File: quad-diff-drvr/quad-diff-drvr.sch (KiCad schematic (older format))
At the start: 43 parts, among them J1 Raspberry_Pi_2_3, J2 Conn_01x04, J3 Conn_01x04, J4 Conn_01x04, J5 Conn_01x04, J6 Conn_01x04, U1 INA3221, U2 74LS153, U3 74LS153, U4 74LS153, U5 PCA9555PW

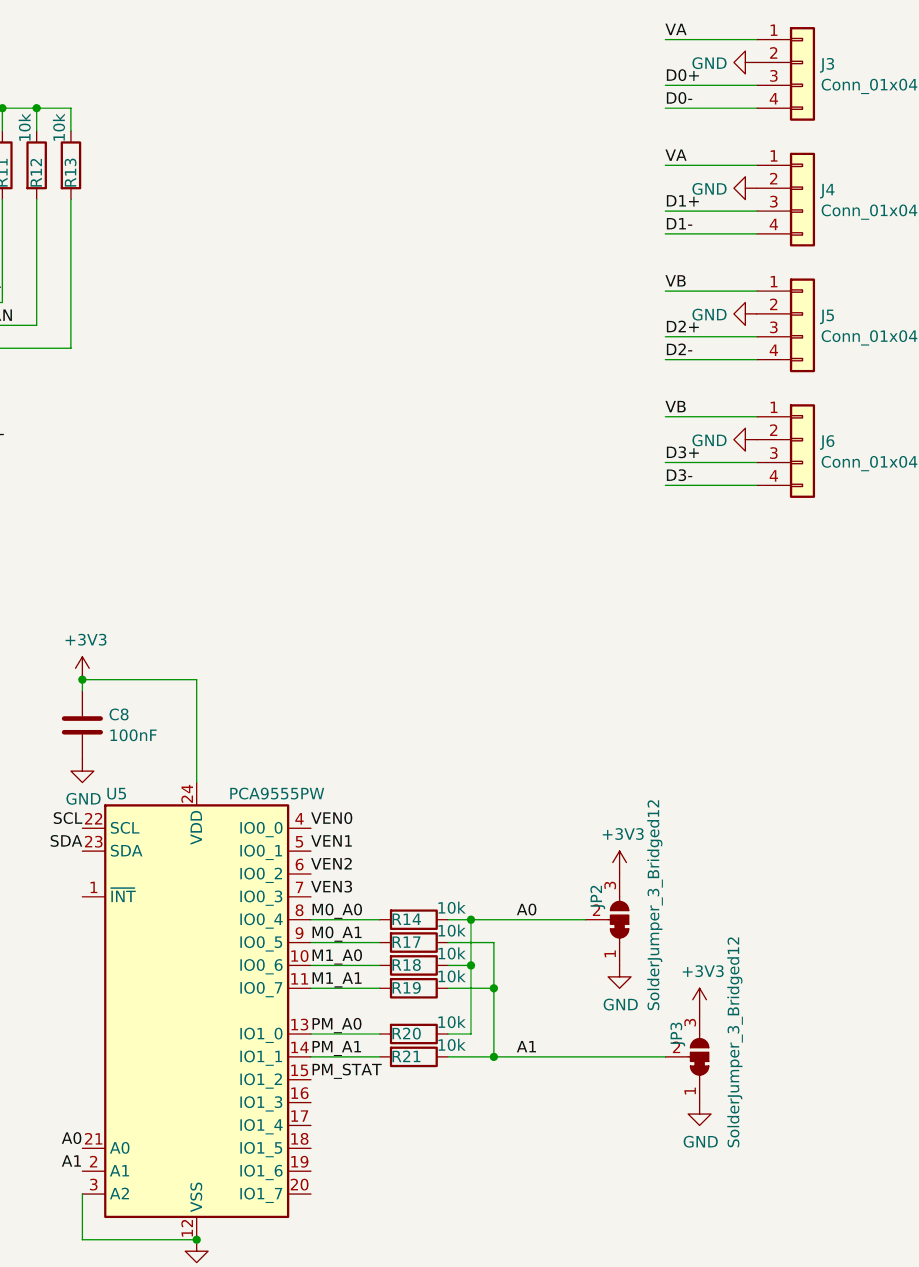
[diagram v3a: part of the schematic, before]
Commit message: qdd: driver added
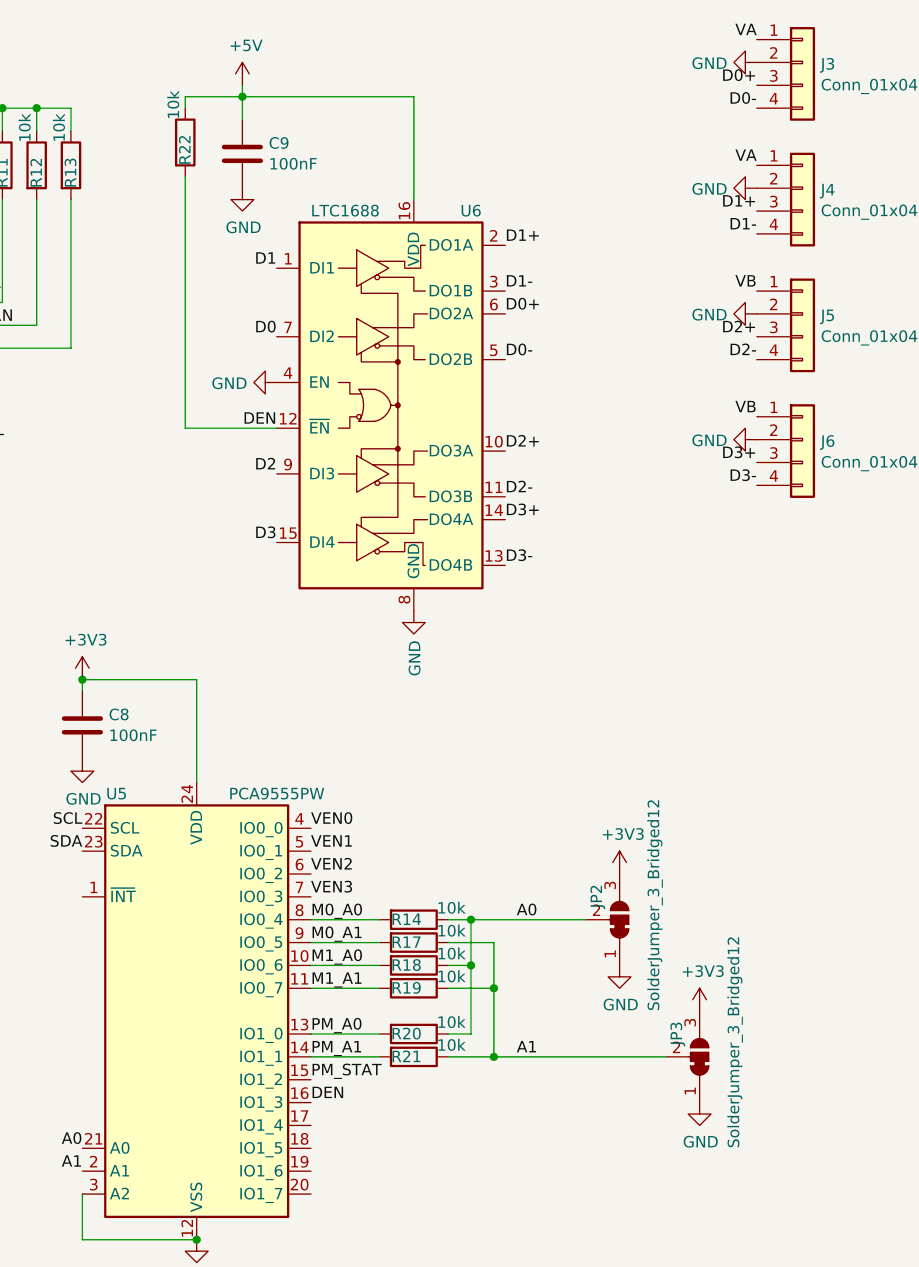
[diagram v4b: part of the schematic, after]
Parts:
- added C9: 100nF, Capacitor_SMD:C_0603_1608Metric, symbol Device:C
- added R22: 10k, Resistor_SMD:R_0603_1608Metric, symbol Device:R
- added U6: LTC1688, Package_SO:SOIC-16_3.9x9.9mm_P1.27mm, symbol Interface:LTC1688
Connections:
- net +5V: now also C9.1, R22.1, U6.16 (VDD)
- net D0: now also U6.7 (DI2)
- net D0+: now also U6.6 (DO2A)
- net D0-: now also U6.5 (DO2B)
- net D1: now also U6.1 (DI1)
- net D1+: now also U6.2 (DO1A)
- net D1-: now also U6.3 (DO1B)
- net D2: now also U6.9 (DI3)
- net D2+: now also U6.10 (DO3A)
- net D2-: now also U6.11 (DO3B)
- net D3: now also U6.15 (DI4)
- net D3+: now also U6.14 (DO4A)
- net D3-: now also U6.13 (DO4B)
- net GND: now also C9.2, U6.4 (EN), U6.8 (GND)
- net DEN: now reaches U5.16 (IO1_3)
- net DEN: now also R22.2, U6.12 (~EN)
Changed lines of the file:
@@
 Wire Wire Line
 	3700 850  3700 950
-Wire Wire Line
-	10750 650  10350 650
-Text Label 10350 650  0    50   ~ 0
+Text Label 10750 650  2    50   ~ 0
 VA
-Wire Wire Line
-	10750 850  10350 850
-Text Label 10350 850  0    50   ~ 0
+Text Label 10750 850  2    50   ~ 0
 D0+
-Wire Wire Line
-	10750 950  10350 950
-Text Label 10350 950  0    50   ~ 0
+Text Label 10750 950  2    50   ~ 0
 D0-
 $Comp
@@
 	0    1    1    0
 $EndComp
-Wire Wire Line
-	10750 1200 10350 1200
-Text Label 10350 1200 0    50   ~ 0
+Text Label 10750 1200 2    50   ~ 0
 VA
-Wire Wire Line
-	10750 1400 10350 1400
-Text Label 10350 1400 0    50   ~ 0
+Text Label 10750 1400 2    50   ~ 0
 D1+
-Wire Wire Line
-	10750 1500 10350 1500
-Text Label 10350 1500 0    50   ~ 0
+Text Label 10750 1500 2    50   ~ 0
 D1-
 $Comp
@@
 	0    1    1    0
 $EndComp
-Wire Wire Line
-	10750 1750 10350 1750
-Text Label 10350 1750 0    50   ~ 0
+Text Label 10750 1750 2    50   ~ 0
 VB
-Wire Wire Line
-	10750 1950 10350 1950
-Text Label 10350 1950 0    50   ~ 0
+Text Label 10750 1950 2    50   ~ 0
 D2+
-Wire Wire Line
-	10750 2050 10350 2050
-Text Label 10350 2050 0    50   ~ 0
+Text Label 10750 2050 2    50   ~ 0
 D2-
 $Comp
@@
 	0    1    1    0
 $EndComp
-Wire Wire Line
-	10750 2300 10350 2300
-Text Label 10350 2300 0    50   ~ 0
+Text Label 10750 2300 2    50   ~ 0
 VB
-Wire Wire Line
-	10750 2500 10350 2500
-Text Label 10350 2500 0    50   ~ 0
+Text Label 10750 2500 2    50   ~ 0
 D3+
-Wire Wire Line
-	10750 2600 10350 2600
-Text Label 10350 2600 0    50   ~ 0
+Text Label 10750 2600 2    50   ~ 0
 D3-
 $Comp
@@
 Text Label 9700 5100 0    50   ~ 0
 A1
+$Comp
+L Interface:LTC1688 U6
+U 1 1 61ED37CD
+P 9150 2250
+F 0 "U6" H 9500 3100 50  0000 C CNN
+F 1 "LTC1688" H 8950 3100 50  0000 C CNN
+F 2 "Package_SO:SOIC-16_3.9x9.9mm_P1.27mm" H 10150 1400 50  0001 C CNN
+F 3 "https://www.analog.com/media/en/technical-documentation/data-sheets/16889fa.pdf" H 9150 2150 50  0001 C CNN
+	1    9150 2250
+	1    0    0    -1
+$EndComp
+Text Label 8800 5300 0    50   ~ 0
+DEN
+Text Label 8650 2350 2    50   ~ 0
+DEN
+Text Label 9650 1550 0    50   ~ 0
+D1+
+Text Label 9650 1750 0    50   ~ 0
+D1-
+Text Label 9650 1850 0    50   ~ 0
+D0+
+Text Label 9650 2050 0    50   ~ 0
+D0-
+Text Label 9650 2450 0    50   ~ 0
+D2+
+Text Label 9650 2650 0    50   ~ 0
+D2-
+Text Label 9650 2750 0    50   ~ 0
+D3+
+Text Label 9650 2950 0    50   ~ 0
+D3-
+$Comp
+L power:GND #PWR0136
+U 1 1 61F139AF
+P 9250 3150
+F 0 "#PWR0136" H 9250 2900 50  0001 C CNN
+F 1 "GND" V 9255 3022 50  0000 R CNN
+F 2 "" H 9250 3150 50  0001 C CNN
+F 3 "" H 9250 3150 50  0001 C CNN
+	1    9250 3150
+	1    0    0    -1
+$EndComp
+$Comp
+L power:GND #PWR0137
+U 1 1 61F13FCA
+P 8650 2150
+F 0 "#PWR0137" H 8650 1900 50  0001 C CNN
+F 1 "GND" V 8655 2022 50  0000 R CNN
+F 2 "" H 8650 2150 50  0001 C CNN
+F 3 "" H 8650 2150 50  0001 C CNN
+	1    8650 2150
+	0    1    1    0
+$EndComp
+$Comp
+L Device:C C9
+U 1 1 61F15C69
+P 8500 1150
+F 0 "C9" H 8615 1196 50  0000 L CNN
+F 1 "100nF" H 8615 1105 50  0000 L CNN
+F 2 "Capacitor_SMD:C_0603_1608Metric" H 8538 1000 50  0001 C CNN
+F 3 "~" H 8500 1150 50  0001 C CNN
+	1    8500 1150
+	1    0    0    -1
+$EndComp
+$Comp
+L power:GND #PWR0138
+U 1 1 61F164E1
+P 8500 1300
+F 0 "#PWR0138" H 8500 1050 50  0001 C CNN
+F 1 "GND" H 8505 1127 50  0000 C CNN
+F 2 "" H 8500 1300 50  0001 C CNN
+F 3 "" H 8500 1300 50  0001 C CNN
+	1    8500 1300
+	1    0    0    -1
+$EndComp
+Wire Wire Line
+	9250 1350 9250 900
+Wire Wire Line
+	9250 900  8500 900
+Wire Wire Line
+	8500 900  8500 1000
+$Comp
+L power:+5V #PWR0139
+U 1 1 61F35BF0
+P 8500 850
+F 0 "#PWR0139" H 8500 700 50  0001 C CNN
+F 1 "+5V" H 8515 1023 50  0000 C CNN
+F 2 "" H 8500 850 50  0001 C CNN
+F 3 "" H 8500 850 50  0001 C CNN
+	1    8500 850
+	1    0    0    -1
+$EndComp
+Wire Wire Line
+	8500 850  8500 900
+Connection ~ 8500 900
+Text Label 8650 1650 2    50   ~ 0
+D1
+Text Label 8650 1950 2    50   ~ 0
+D0
+Text Label 8650 2550 2    50   ~ 0
+D2
+Text Label 8650 2850 2    50   ~ 0
+D3
+$Comp
+L Device:R R22
+U 1 1 61F5B30A
+P 8250 1100
+F 0 "R22" V 8250 1000 50  0000 L CNN
+F 1 "10k" V 8200 1200 50  0000 L CNN
+F 2 "Resistor_SMD:R_0603_1608Metric" V 8180 1100 50  0001 C CNN
+F 3 "~" H 8250 1100 50  0001 C CNN
+	1    8250 1100
+	1    0    0    -1
+$EndComp
+Wire Wire Line
+	8500 900  8250 900
+Wire Wire Line
+	8250 900  8250 950
+Wire Wire Line
+	8650 2350 8250 2350
+Wire Wire Line
+	8250 2350 8250 1250
 $EndSCHEMATC

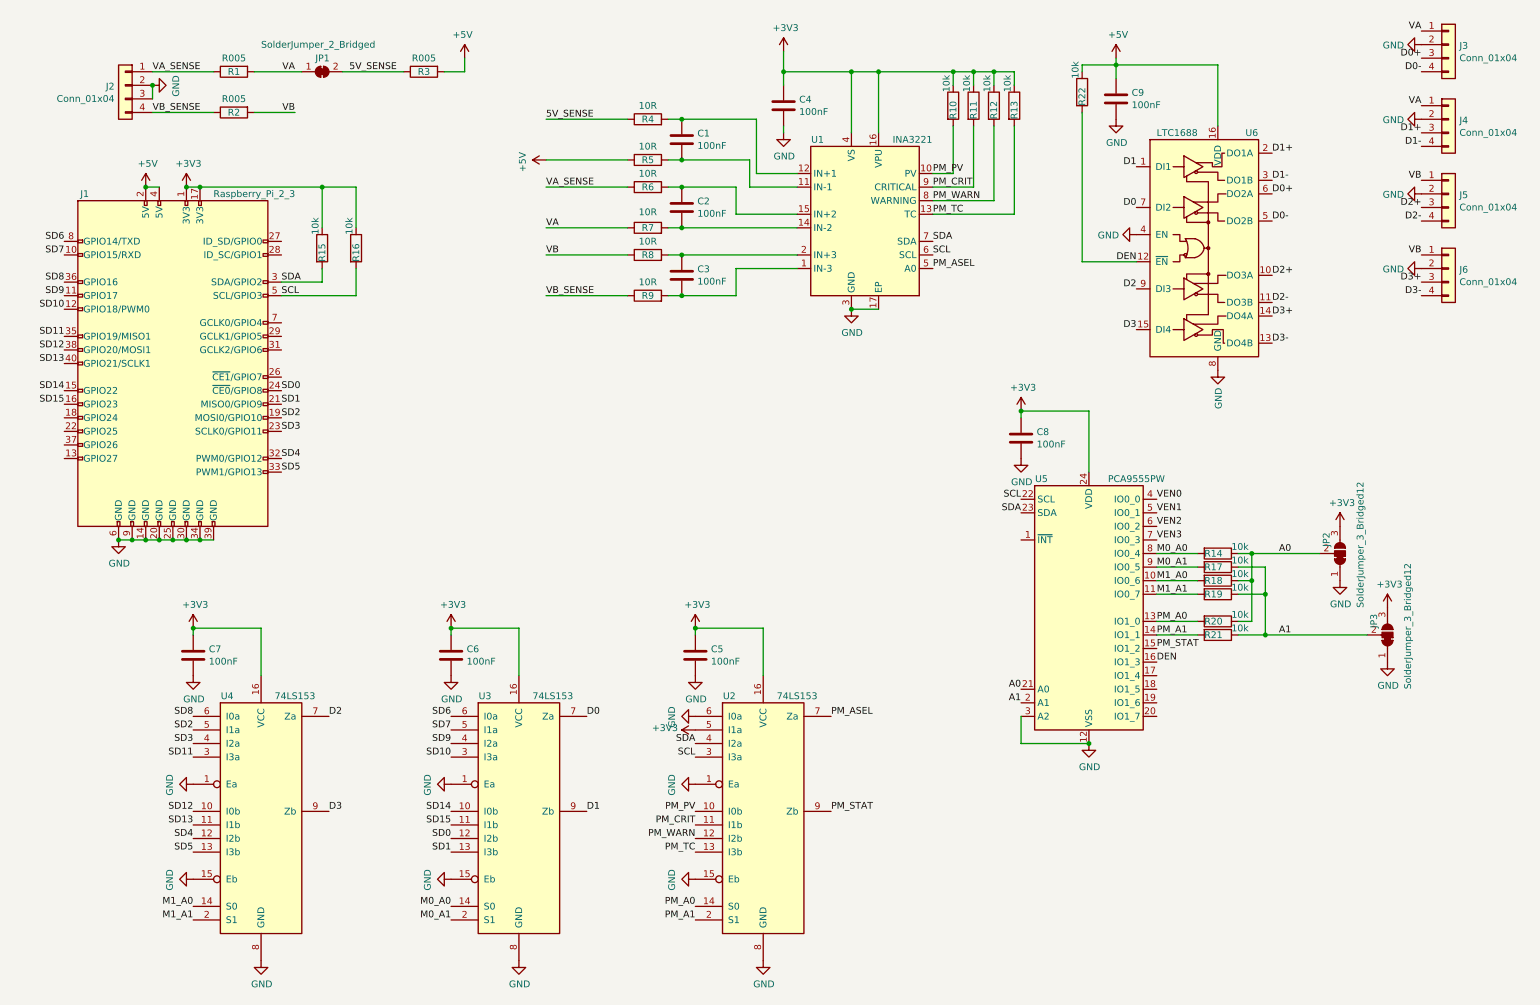
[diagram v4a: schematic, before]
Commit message: qdd: first pass at routing
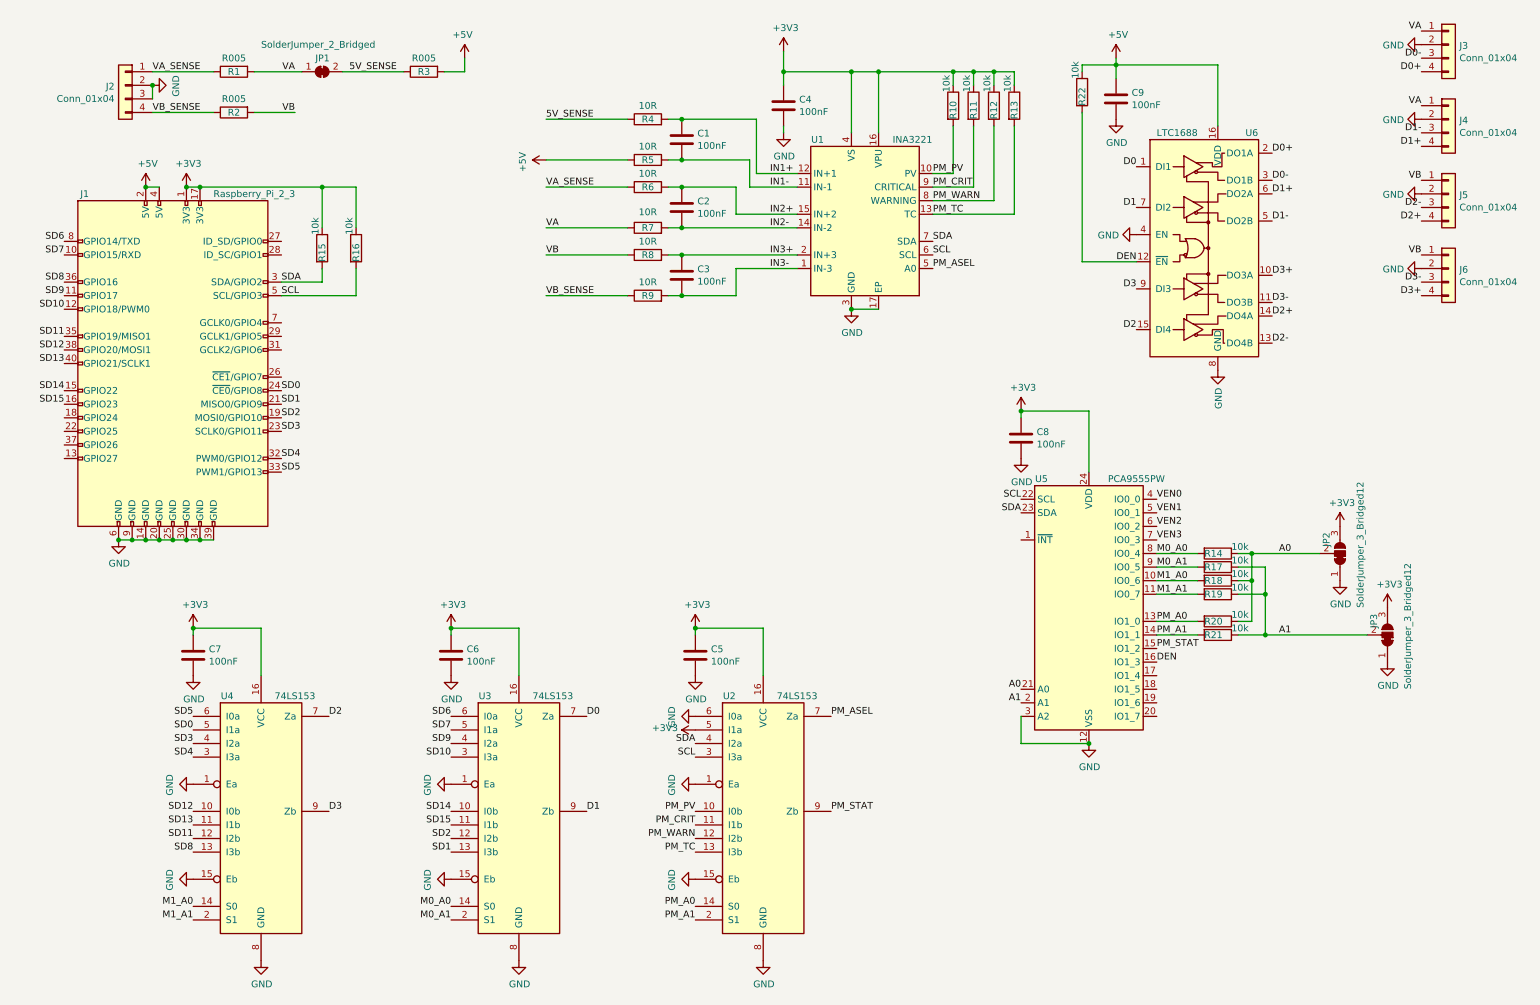
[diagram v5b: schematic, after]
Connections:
- net D0: now also U6.1 (DI1); no longer U6.7 (DI2)
- net D0+: now also J3.4 (Pin_4), U6.2 (DO1A); no longer J3.3 (Pin_3), U6.6 (DO2A)
- net D0-: now also J3.3 (Pin_3), U6.3 (DO1B); no longer J3.4 (Pin_4), U6.5 (DO2B)
- net D1: now also U6.7 (DI2); no longer U6.1 (DI1)
- net D1+: now also J4.4 (Pin_4), U6.6 (DO2A); no longer J4.3 (Pin_3), U6.2 (DO1A)
- net D1-: now also J4.3 (Pin_3), U6.5 (DO2B); no longer J4.4 (Pin_4), U6.3 (DO1B)
- net D2: now also U6.15 (DI4); no longer U6.9 (DI3)
- net D2+: now also J5.4 (Pin_4), U6.14 (DO4A); no longer J5.3 (Pin_3), U6.10 (DO3A)
- net D2-: now also J5.3 (Pin_3), U6.13 (DO4B); no longer J5.4 (Pin_4), U6.11 (DO3B)
- net D3: now also U6.9 (DI3); no longer U6.15 (DI4)
- net D3+: now also J6.4 (Pin_4), U6.10 (DO3A); no longer J6.3 (Pin_3), U6.14 (DO4A)
- net D3-: now also J6.3 (Pin_3), U6.11 (DO3B); no longer J6.4 (Pin_4), U6.13 (DO4B)
- net SD0: now also U4.5 (I1a); no longer U3.12 (I2b)
- net SD11: now also U4.12 (I2b); no longer U4.3 (I3a)
- net SD2: now also U3.12 (I2b); no longer U4.5 (I1a)
- net SD4: now also U4.3 (I3a); no longer U4.12 (I2b)
- net SD5: now also U4.6 (I0a); no longer U4.13 (I3b)
- net SD8: now also U4.13 (I3b); no longer U4.6 (I0a)
- net IN3-: now reaches C3.2, R9.2, U1.1 (IN-3)
- net IN1-: now reaches C1.2, R5.2, U1.11 (IN-1)
- net IN1+: now reaches C1.1, R4.2, U1.12 (IN+1)
- net IN2-: now reaches C2.2, R7.2, U1.14 (IN-2)
- net IN2+: now reaches C2.1, R6.2, U1.15 (IN+2)
- net IN3+: now reaches C3.1, R8.2, U1.2 (IN+3)
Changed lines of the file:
@@
 Text Label 10750 650  2    50   ~ 0
 VA
+Text Label 10750 950  2    50   ~ 0
+D0+
 Text Label 10750 850  2    50   ~ 0
-D0+
-Text Label 10750 950  2    50   ~ 0
 D0-
 $Comp
@@
 Text Label 10750 1200 2    50   ~ 0
 VA
+Text Label 10750 1500 2    50   ~ 0
+D1+
 Text Label 10750 1400 2    50   ~ 0
-D1+
-Text Label 10750 1500 2    50   ~ 0
 D1-
 $Comp
@@
 Text Label 10750 1750 2    50   ~ 0
 VB
+Text Label 10750 2050 2    50   ~ 0
+D2+
 Text Label 10750 1950 2    50   ~ 0
-D2+
-Text Label 10750 2050 2    50   ~ 0
 D2-
 $Comp
@@
 Text Label 10750 2300 2    50   ~ 0
 VB
+Text Label 10750 2600 2    50   ~ 0
+D3+
 Text Label 10750 2500 2    50   ~ 0
-D3+
-Text Label 10750 2600 2    50   ~ 0
 D3-
 $Comp
@@
 Text Label 750  2200 2    50   ~ 0
 SD6
-Text Label 3600 6600 2    50   ~ 0
+Text Label 1700 5800 2    50   ~ 0
 SD0
 Text Label 3600 6700 2    50   ~ 0
 SD1
-Text Label 1700 5800 2    50   ~ 0
+Text Label 3600 6600 2    50   ~ 0
 SD2
 Text Label 1700 5900 2    50   ~ 0
 SD3
-Text Label 1700 6600 2    50   ~ 0
+Text Label 1700 6000 2    50   ~ 0
 SD4
-Text Label 1700 6700 2    50   ~ 0
+Text Label 1700 5700 2    50   ~ 0
 SD5
 Text Label 3600 5800 2    50   ~ 0
@@
 Text Label 2700 6400 0    50   ~ 0
 D3
-Text Label 1700 5700 2    50   ~ 0
+Text Label 1700 6700 2    50   ~ 0
 SD8
 Text Label 3600 5900 2    50   ~ 0
@@
 Text Label 3600 6000 2    50   ~ 0
 SD10
-Text Label 1700 6000 2    50   ~ 0
+Text Label 1700 6600 2    50   ~ 0
 SD11
 Text Label 1700 6400 2    50   ~ 0
@@
 Text Label 8650 2350 2    50   ~ 0
 DEN
+Text Label 9650 1850 0    50   ~ 0
+D1+
+Text Label 9650 2050 0    50   ~ 0
+D1-
 Text Label 9650 1550 0    50   ~ 0
-D1+
+D0+
 Text Label 9650 1750 0    50   ~ 0
-D1-
-Text Label 9650 1850 0    50   ~ 0
-D0+
-Text Label 9650 2050 0    50   ~ 0
 D0-
+Text Label 9650 2750 0    50   ~ 0
+D2+
+Text Label 9650 2950 0    50   ~ 0
+D2-
 Text Label 9650 2450 0    50   ~ 0
-D2+
+D3+
 Text Label 9650 2650 0    50   ~ 0
-D2-
-Text Label 9650 2750 0    50   ~ 0
-D3+
-Text Label 9650 2950 0    50   ~ 0
 D3-
 $Comp
@@
 	8500 850  8500 900
 Connection ~ 8500 900
+Text Label 8650 1950 2    50   ~ 0
+D1
 Text Label 8650 1650 2    50   ~ 0
-D1
-Text Label 8650 1950 2    50   ~ 0
 D0
+Text Label 8650 2850 2    50   ~ 0
+D2
 Text Label 8650 2550 2    50   ~ 0
-D2
-Text Label 8650 2850 2    50   ~ 0
 D3
 $Comp
@@
 Wire Wire Line
 	8250 2350 8250 1250
+Text Label 5950 1700 0    50   ~ 0
+IN1+
+Text Label 5950 1800 0    50   ~ 0
+IN1-
+Text Label 5950 2000 0    50   ~ 0
+IN2+
+Text Label 5950 2100 0    50   ~ 0
+IN2-
+Text Label 5950 2300 0    50   ~ 0
+IN3+
+Text Label 5950 2400 0    50   ~ 0
+IN3-
 $EndSCHEMATC
